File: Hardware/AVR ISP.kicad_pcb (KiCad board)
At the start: 2 copper layers, 68.6 x 53.3 mm, 14 parts, among them CON1 AVR-ISP-6, CON2 AVR-ISP-10, IC1 ATMEGA328, IC2 ATTINY2313, IC3 ATTINY85

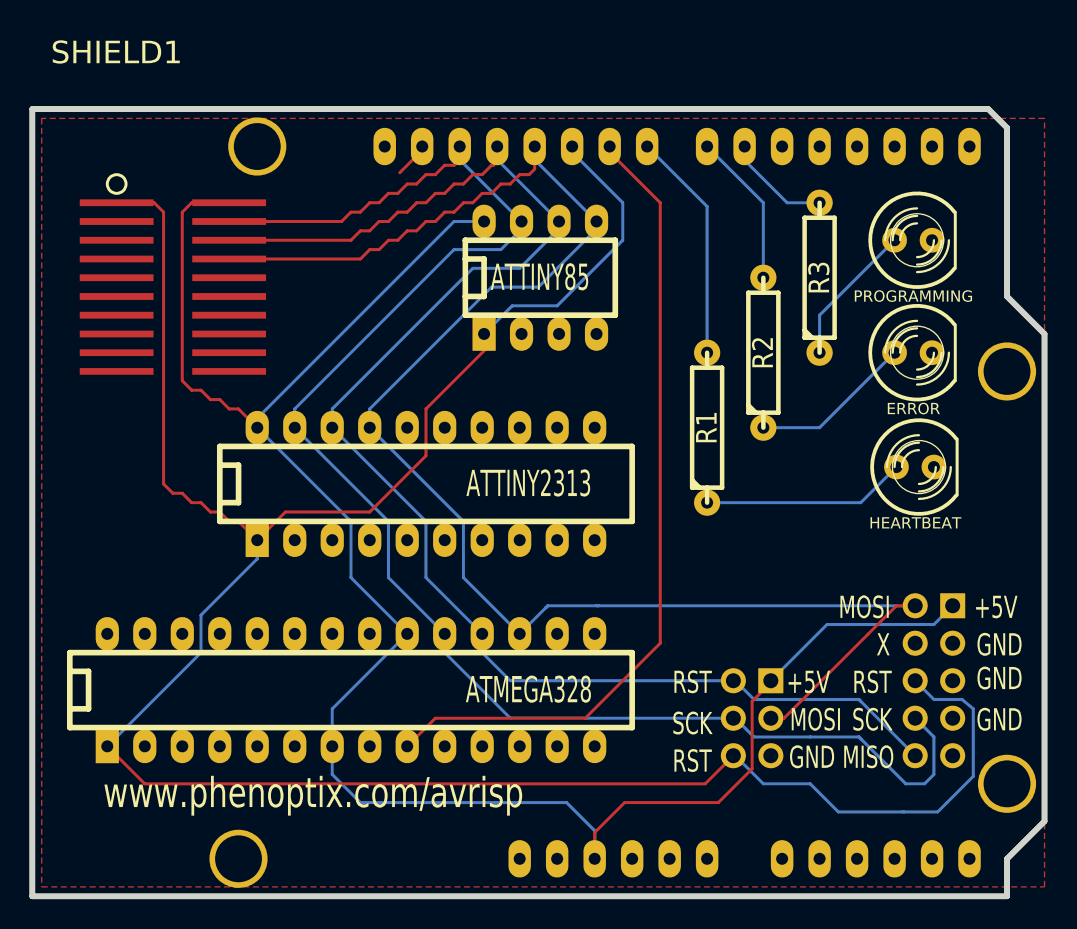
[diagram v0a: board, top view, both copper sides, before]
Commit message: KiCad 10, reset cap, correct LED, opt ext clk
Updated to KiCad 10 project files
Added a capacitor between arduino reset and ground preventing a reset
before programming.
Updated LED pins
Added support for an external clock source

Signed-off-by: Robert Knutsson <zybreak@gmail.com>
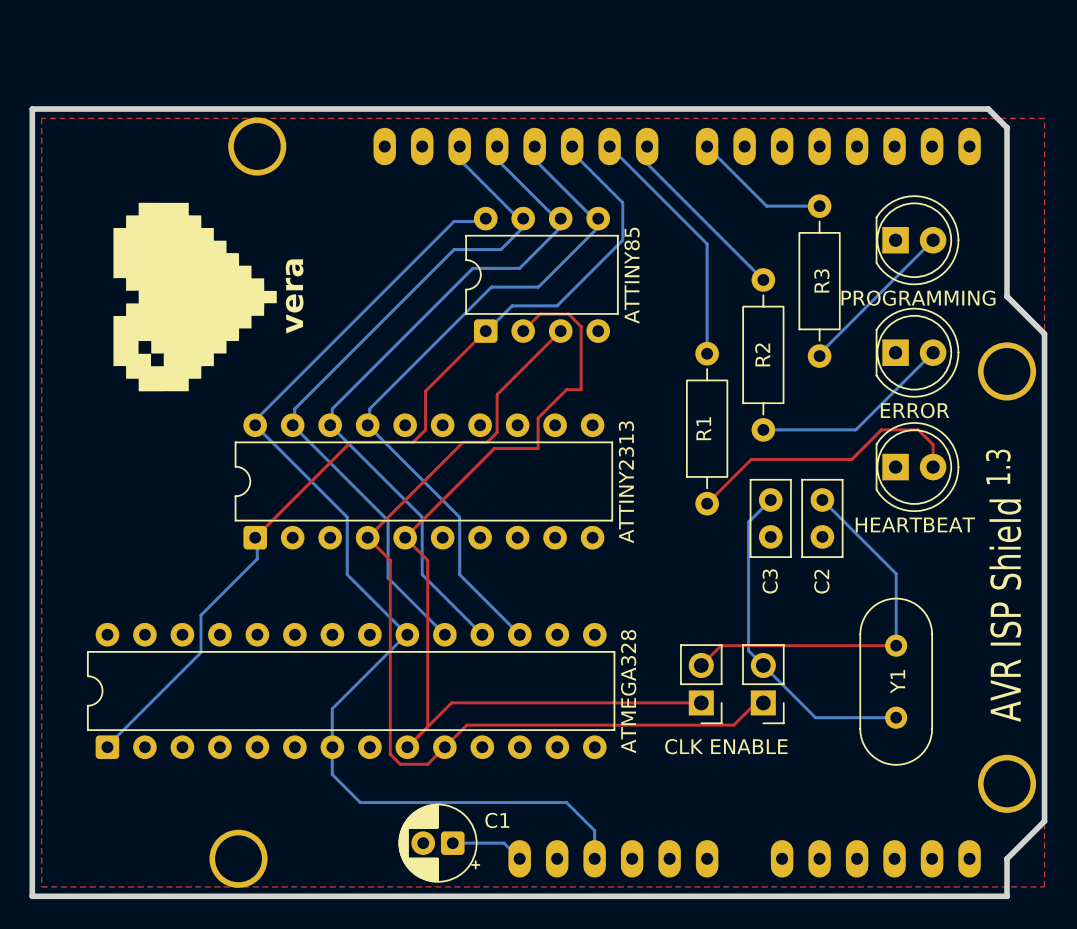
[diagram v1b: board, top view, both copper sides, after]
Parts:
- removed CON1: AVR-ISP-6, pin_array_3x2
- removed CON2: AVR-ISP-10, PIN_ARRAY_5x2
- removed SOIC - 8: Test, SOIC20_Test
- removed VAL: logoBigBackSilk, logoBigBackSilk
- added C1: C_Polarized, Capacitor_THT:CP_Radial_D5.0mm_P2.00mm, F.Cu at (106.0, 98.0)
- added C2: C_Small, Capacitor_THT:C_Disc_D5.0mm_W2.5mm_P2.50mm, F.Cu at (131.0, 74.8)
- added C3: C_Small, Capacitor_THT:C_Disc_D5.0mm_W2.5mm_P2.50mm, F.Cu at (127.5, 74.8)
- added CLK ENABLE: ~, Connector_PinHeader_2.54mm:PinHeader_1x02_P2.54mm_Vertical, F.Cu at (122.8, 88.5)
- added G***: LOGO, LOGO, F.Cu at (88.5, 61.0)
- added JP2: ~, Connector_PinHeader_2.54mm:PinHeader_1x02_P2.54mm_Vertical, F.Cu at (127.0, 88.5)
- added Y1: Crystal, Crystal:Crystal_HC49-4H_Vertical, F.Cu at (136.0, 89.5)
- D1, D2, D3: footprint LED-5MM -> LED_THT:LED_D5.0mm
- IC1: footprint DIP-28__300_ELL -> Package_DIP:DIP-28_W7.62mm
- IC2: footprint DIP-20__300_ELL -> Package_DIP:DIP-20_W7.62mm
- IC3: footprint DIP-8__300_ELL -> Package_DIP:DIP-8_W7.62mm
- R1, R2, R3: value R -> 330; footprint R4-LARGE_PADS -> Resistor_THT:R_Axial_DIN0207_L6.3mm_D2.5mm_P10.16mm_Horizontal
- SHIELD1: footprint ARDUINO_SHIELD -> AVR ISP:ARDUINO_SHIELD
- moved IC1 16.9 mm to (82.6, 91.5), turned to 90 degrees
- moved IC2 12.1 mm to (92.6, 77.3), turned to 90 degrees
- moved R3 5.31 mm to (130.8, 65.0)
- moved R2 5.23 mm to (127.0, 70.0)
- moved IC3 5.17 mm to (108.2, 63.3), turned to 90 degrees
- moved R1 5.15 mm to (123.2, 75.0)
- moved D1 1.33 mm to (136.0, 72.5)
- moved D2 1.20 mm to (136.0, 64.8)
- moved D3 1.20 mm to (136.0, 57.1)
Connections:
- D1 pad 1: N-000062 -> GND
- D1 pad 2: GND -> Net-(D1-A)
- D2 pad 1: N-000064 -> GND
- D2 pad 2: GND -> Net-(D2-A)
- D3 pad 1: N-000060 -> GND
- D3 pad 2: GND -> Net-(D3-A)
- IC1 pad 10: (no net) -> Net-(IC1-XTAL2/PB7)
- IC1 pad 11: (no net) -> unconnected-(IC1-PD5-Pad11)
- IC1 pad 12: (no net) -> unconnected-(IC1-PD6-Pad12)
- IC1 pad 13: (no net) -> unconnected-(IC1-PD7-Pad13)
- IC1 pad 14: (no net) -> unconnected-(IC1-PB0-Pad14)
- IC1 pad 15: (no net) -> unconnected-(IC1-PB1-Pad15)
- IC1 pad 16: (no net) -> unconnected-(IC1-PB2-Pad16)
- IC1 pad 2: (no net) -> unconnected-(IC1-PD0-Pad2)
- IC1 pad 21: (no net) -> unconnected-(IC1-AREF-Pad21)
- IC1 pad 23: (no net) -> unconnected-(IC1-PC0-Pad23)
- IC1 pad 24: (no net) -> unconnected-(IC1-PC1-Pad24)
- IC1 pad 25: (no net) -> unconnected-(IC1-PC2-Pad25)
- IC1 pad 26: (no net) -> unconnected-(IC1-PC3-Pad26)
- IC1 pad 27: (no net) -> unconnected-(IC1-PC4-Pad27)
- IC1 pad 28: (no net) -> unconnected-(IC1-PC5-Pad28)
- IC1 pad 3: (no net) -> unconnected-(IC1-PD1-Pad3)
- IC1 pad 4: (no net) -> unconnected-(IC1-PD2-Pad4)
- IC1 pad 5: (no net) -> unconnected-(IC1-PD3-Pad5)
- IC1 pad 6: (no net) -> unconnected-(IC1-PD4-Pad6)
- IC1 pad 9: N-000073 -> Net-(IC1-XTAL1/PB6)
- IC2 pad 11: (no net) -> unconnected-(IC2-PD6-Pad11)
- IC2 pad 12: (no net) -> unconnected-(IC2-PB0-Pad12)
- IC2 pad 13: (no net) -> unconnected-(IC2-PB1-Pad13)
- IC2 pad 14: (no net) -> unconnected-(IC2-PB2-Pad14)
- IC2 pad 15: (no net) -> unconnected-(IC2-PB3-Pad15)
- IC2 pad 16: (no net) -> unconnected-(IC2-PB4-Pad16)
- IC2 pad 2: (no net) -> unconnected-(IC2-PD0-Pad2)
- IC2 pad 3: (no net) -> unconnected-(IC2-PD1-Pad3)
- IC2 pad 4: (no net) -> Net-(IC1-XTAL2/PB7)
- IC2 pad 5: (no net) -> Net-(IC1-XTAL1/PB6)
- IC2 pad 6: (no net) -> unconnected-(IC2-PD2-Pad6)
- IC2 pad 7: (no net) -> unconnected-(IC2-PD3-Pad7)
- IC2 pad 8: (no net) -> unconnected-(IC2-PD4-Pad8)
- IC2 pad 9: (no net) -> unconnected-(IC2-PD5-Pad9)
- IC3 pad 2: (no net) -> Net-(IC1-XTAL1/PB6)
- IC3 pad 3: (no net) -> Net-(IC1-XTAL2/PB7)
- R1 pad 1: N-000062 -> Net-(D1-A)
- R1 pad 2: N-000061 -> Net-(R1-Pad2)
- R2 pad 1: N-000064 -> Net-(D2-A)
- R2 pad 2: N-000063 -> Net-(R2-Pad2)
- R3 pad 1: N-000060 -> Net-(D3-A)
- R3 pad 2: N-000037 -> Net-(R3-Pad2)
- SHIELD1 pad 0: (no net) -> unconnected-(SHIELD1-Pad0)
- SHIELD1 pad 1: (no net) -> unconnected-(SHIELD1-Pad1)
- SHIELD1 pad 2: (no net) -> unconnected-(SHIELD1-Pad2)
- SHIELD1 pad 3: (no net) -> unconnected-(SHIELD1-Pad3)
- SHIELD1 pad 3V3: (no net) -> unconnected-(SHIELD1-Pad3V3)
- SHIELD1 pad 4: (no net) -> unconnected-(SHIELD1-Pad4)
- SHIELD1 pad 5: (no net) -> unconnected-(SHIELD1-Pad5)
- SHIELD1 pad 6: N-000037 -> unconnected-(SHIELD1-Pad6)
- SHIELD1 pad 7: N-000063 -> Net-(R3-Pad2)
- SHIELD1 pad 8: N-000061 -> Net-(R2-Pad2)
- SHIELD1 pad 9: N-000073 -> Net-(R1-Pad2)
- SHIELD1 pad AD0: (no net) -> unconnected-(SHIELD1-PadAD0)
- SHIELD1 pad AD1: (no net) -> unconnected-(SHIELD1-PadAD1)
- SHIELD1 pad AD2: (no net) -> unconnected-(SHIELD1-PadAD2)
- SHIELD1 pad AD3: (no net) -> unconnected-(SHIELD1-PadAD3)
- SHIELD1 pad AD4: (no net) -> unconnected-(SHIELD1-PadAD4)
- SHIELD1 pad AD5: (no net) -> unconnected-(SHIELD1-PadAD5)
- SHIELD1 pad AREF: (no net) -> unconnected-(SHIELD1-PadAREF)
- SHIELD1 pad RST: (no net) -> Net-(C1-Pad1)
- SHIELD1 pad V_IN: (no net) -> unconnected-(SHIELD1-PadV_IN)
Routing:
- net Net-(IC1-~{RESET}/PC6): track 163.8 -> 60.5 mm
- net Net-(IC1-PB3): track 112.8 -> 46.1 mm
- net Net-(IC1-XTAL1/PB6): track 0.00 -> 62.9 mm
- net Net-(IC1-XTAL2/PB7): track 0.00 -> 62.5 mm
- net Net-(IC1-PB5): track 108.3 -> 46.1 mm
- net +5V: track 130.9 -> 72.2 mm
- net Net-(IC1-PB4): track 102.4 -> 46.1 mm
- net N-000073: track 55.1 -> 0.00 mm
- net Net-(JP1-B): track 0.00 -> 25.7 mm
- net Net-(JP2-B): track 0.00 -> 22.7 mm
- net Net-(D1-A): track 0.00 -> 19.3 mm
- net Net-(R1-Pad2): track 0.00 -> 16.8 mm
- net N-000061: track 15.7 -> 0.00 mm
- net N-000062: track 13.8 -> 0.00 mm
- net Net-(D2-A): track 0.00 -> 13.7 mm
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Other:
- net class Default removed
- rule pad_to_mask_clearance: 0.254 -> 0.05
- rule solder_mask_min_width: 0.25 -> 0.12
- board text added: "AVR ISP Shield ^{1.3}"
- board text added: "vera"
- board text removed: "+5V"
- board text removed: "AVRISP Shield v1.1"
- board text removed: "GND"
- board text removed: "MISO"
- board text removed: "MOSI"
- board text removed: "RST"
- board text removed: "SCK"
- board text removed: "X"
- board text removed: "www.phenoptix.com/avrisp"
- board text removed: "www.phenoptix.com/avrisp CC BY-SA 3.0"
